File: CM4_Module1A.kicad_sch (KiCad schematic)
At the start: 1 part

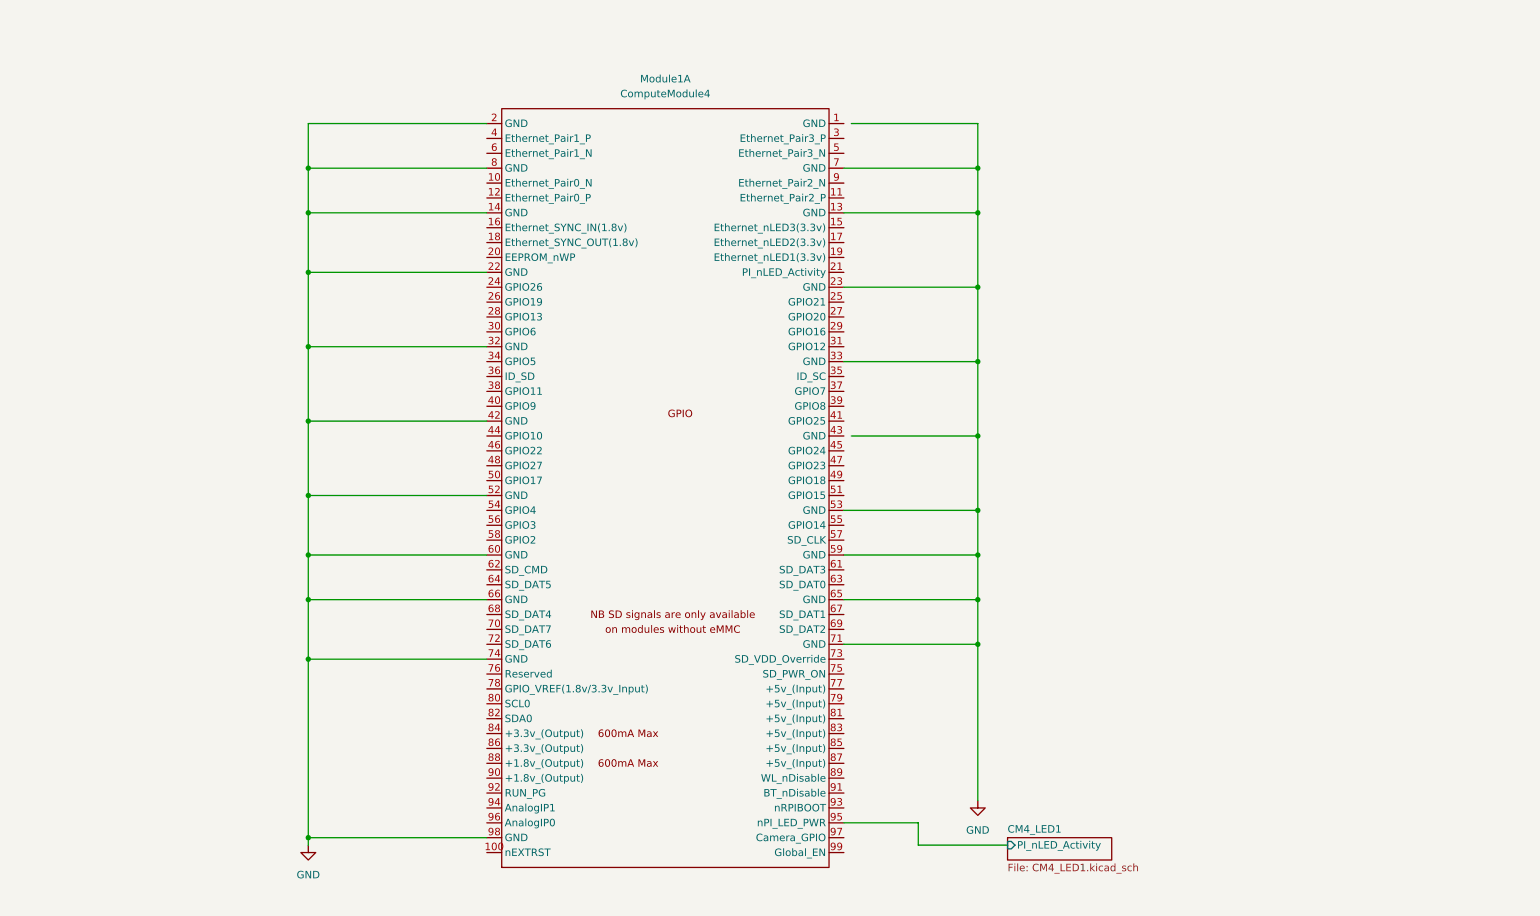
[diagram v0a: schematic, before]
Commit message: added gitignore, and did work on CM4
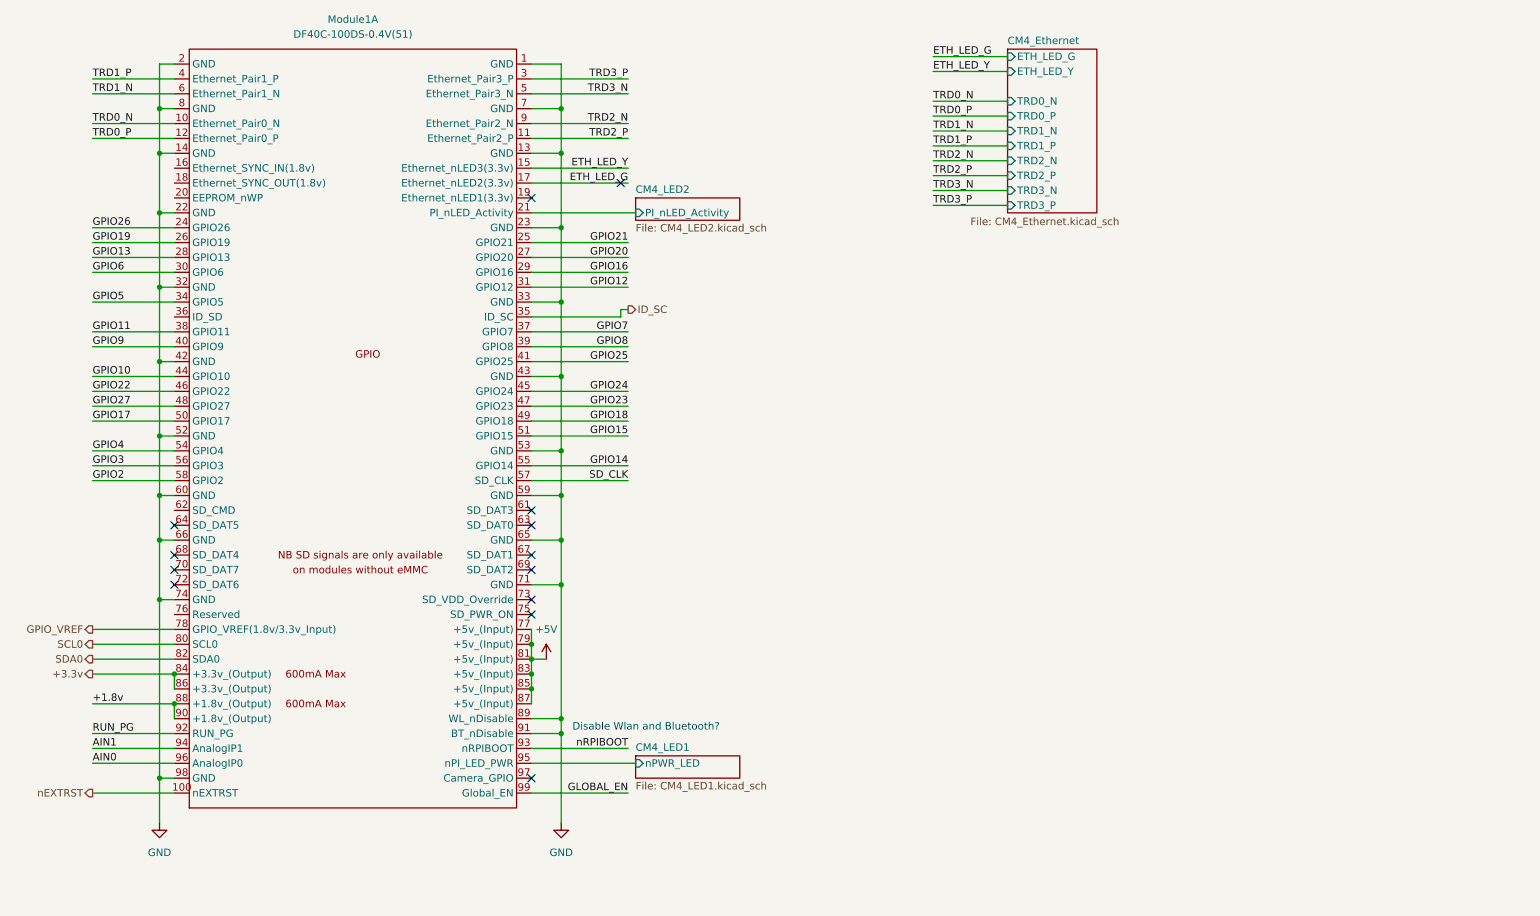
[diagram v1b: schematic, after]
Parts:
- removed Module1: ComputeModule4, CM4IO:Raspberry-Pi-4-Compute-Module, symbol dz_con:DF40C-100DS-0.4V_51_
- added Module1: DF40C-100DS-0.4V(51), dz_con:Con-Raspberry-Pi-4-Compute-Module, symbol #dzdb:s_con/CON-DF40C-100DS-0.4V51
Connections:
- net GND: now also Module1.1 (GND), Module1.13 (GND), Module1.14 (GND), Module1.2 (GND), Module1.22 (GND), Module1.23 (GND), Module1.32 (GND), Module1.33 (GND), Module1.42 (GND), Module1.43 (GND), Module1.52 (GND), Module1.53 (GND), Module1.59 (GND), Module1.60 (GND), Module1.65 (GND), Module1.66 (GND), Module1.7 (GND), Module1.71 (GND), Module1.74 (GND), Module1.8 (GND), Module1.89 (WL_nDisable), Module1.91 (BT_nDisable), Module1.98 (GND)
- new net +1.8v: Module1.88 (+1.8v_(Output)), Module1.90 (+1.8v_(Output))
- new net +3.3v: Module1.84 (+3.3v_(Output)), Module1.86 (+3.3v_(Output))
- new net +5V: Module1.77 (+5v_(Input)), Module1.79 (+5v_(Input)), Module1.81 (+5v_(Input)), Module1.83 (+5v_(Input)), Module1.85 (+5v_(Input)), Module1.87 (+5v_(Input))
- new net AIN0: Module1.96 (AnalogIP0)
- new net AIN1: Module1.94 (AnalogIP1)
- new net CM4_LED1/nPWR_LED: Module1.95 (nPI_LED_PWR)
- new net CM4_LED2/PI_nLED_Activity: Module1.21 (PI_nLED_Activity)
- new net ETH_LED_G: Module1.17 (Ethernet_nLED2(3.3v))
- new net ETH_LED_Y: Module1.15 (Ethernet_nLED3(3.3v))
- new net GLOBAL_EN: Module1.99 (Global_EN)
- new net GPIO10: Module1.44 (GPIO10)
- new net GPIO11: Module1.38 (GPIO11)
- new net GPIO12: Module1.31 (GPIO12)
- new net GPIO13: Module1.28 (GPIO13)
- new net GPIO14: Module1.55 (GPIO14)
- new net GPIO15: Module1.51 (GPIO15)
- new net GPIO16: Module1.29 (GPIO16)
- new net GPIO17: Module1.50 (GPIO17)
- new net GPIO18: Module1.49 (GPIO18)
- new net GPIO19: Module1.26 (GPIO19)
- new net GPIO2: Module1.58 (GPIO2)
- new net GPIO20: Module1.27 (GPIO20)
- new net GPIO21: Module1.25 (GPIO21)
- new net GPIO22: Module1.46 (GPIO22)
- new net GPIO23: Module1.47 (GPIO23)
- new net GPIO24: Module1.45 (GPIO24)
- new net GPIO25: Module1.41 (GPIO25)
- new net GPIO26: Module1.24 (GPIO26)
- new net GPIO27: Module1.48 (GPIO27)
- new net GPIO3: Module1.56 (GPIO3)
- new net GPIO4: Module1.54 (GPIO4)
- new net GPIO5: Module1.34 (GPIO5)
- new net GPIO6: Module1.30 (GPIO6)
- new net GPIO7: Module1.37 (GPIO7)
- new net GPIO8: Module1.39 (GPIO8)
- new net GPIO9: Module1.40 (GPIO9)
- new net GPIO_VREF: Module1.78 (GPIO_VREF(1.8v/3.3v_Input))
- new net ID_SC: Module1.35 (ID_SC)
- new net RUN_PG: Module1.92 (RUN_PG)
- new net SCL0: Module1.80 (SCL0)
- new net SDA0: Module1.82 (SDA0)
- new net SD_CLK: Module1.57 (SD_CLK)
- new net TRD0_N: Module1.10 (Ethernet_Pair0_N)
- new net TRD0_P: Module1.12 (Ethernet_Pair0_P)
- new net TRD1_N: Module1.6 (Ethernet_Pair1_N)
- new net TRD1_P: Module1.4 (Ethernet_Pair1_P)
- new net TRD2_N: Module1.9 (Ethernet_Pair2_N)
- new net TRD2_P: Module1.11 (Ethernet_Pair2_P)
- new net TRD3_N: Module1.5 (Ethernet_Pair3_N)
- new net TRD3_P: Module1.3 (Ethernet_Pair3_P)
- new net nEXTRST: Module1.100 (nEXTRST)
- new net nRPIBOOT: Module1.93 (nRPIBOOT)
- no-connect marks 0 -> 13
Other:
- added sheet CM4_Ethernet (CM4_Ethernet.kicad_sch)
- added sheet CM4_LED2 (CM4_LED2.kicad_sch)
- sheet CM4_LED1 ports: added nPWR_LED; removed PI_nLED_Activity
- note added: "Disable Wlan and Bluetooth?"

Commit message: minor changes/cleanup
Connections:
- net +1.8v renamed +1V8
- net +3.3v renamed +3.3V
- net TRD0_N renamed ET1
- net TRD0_P renamed ET2
- net TRD1_N renamed ET3
- net TRD1_P renamed ET4
- net TRD2_N renamed ET5
- net TRD2_P renamed ET6
- net TRD3_N renamed ET7
- net TRD3_P renamed ET8
- no-connect marks 13 -> 12

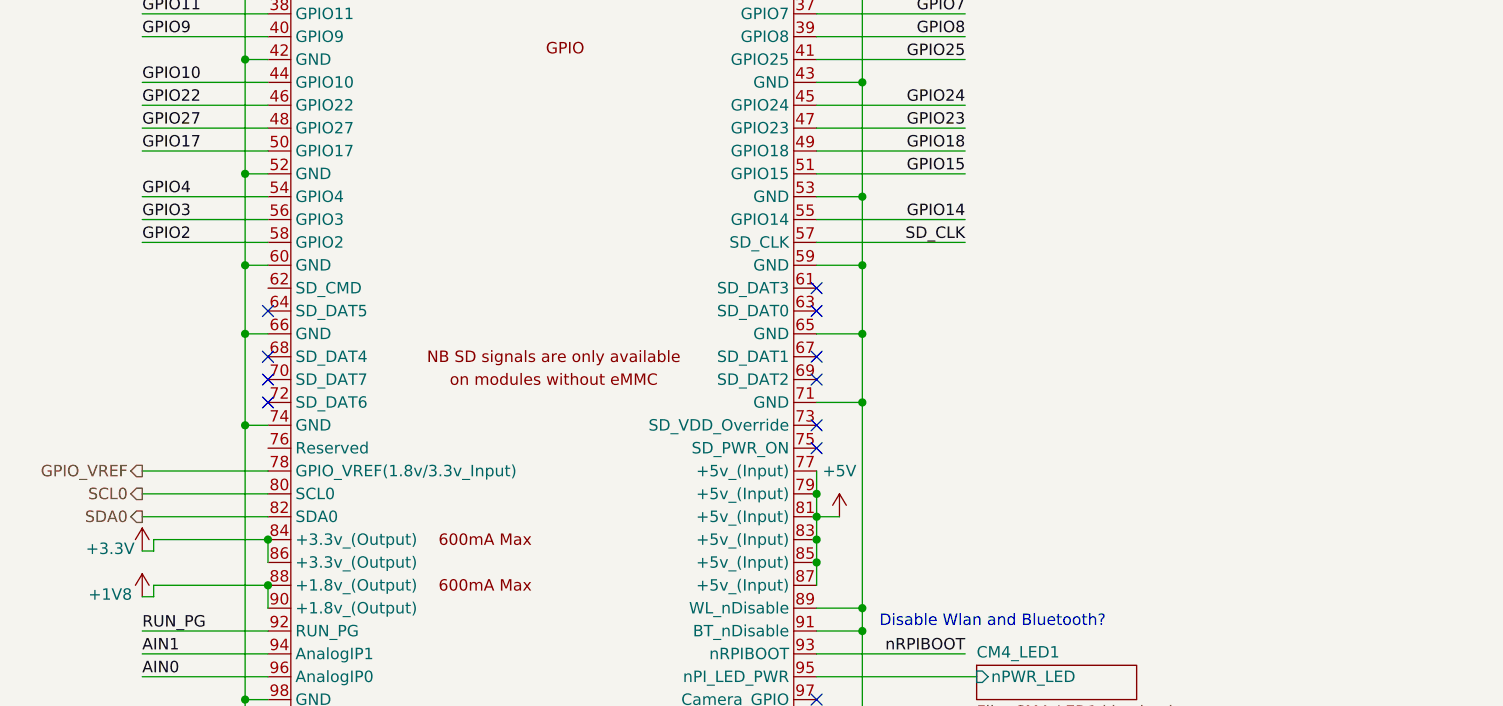
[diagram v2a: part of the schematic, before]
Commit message: readded RX and TX, Corrected DZ_PATHS to be relative instead of absolute.
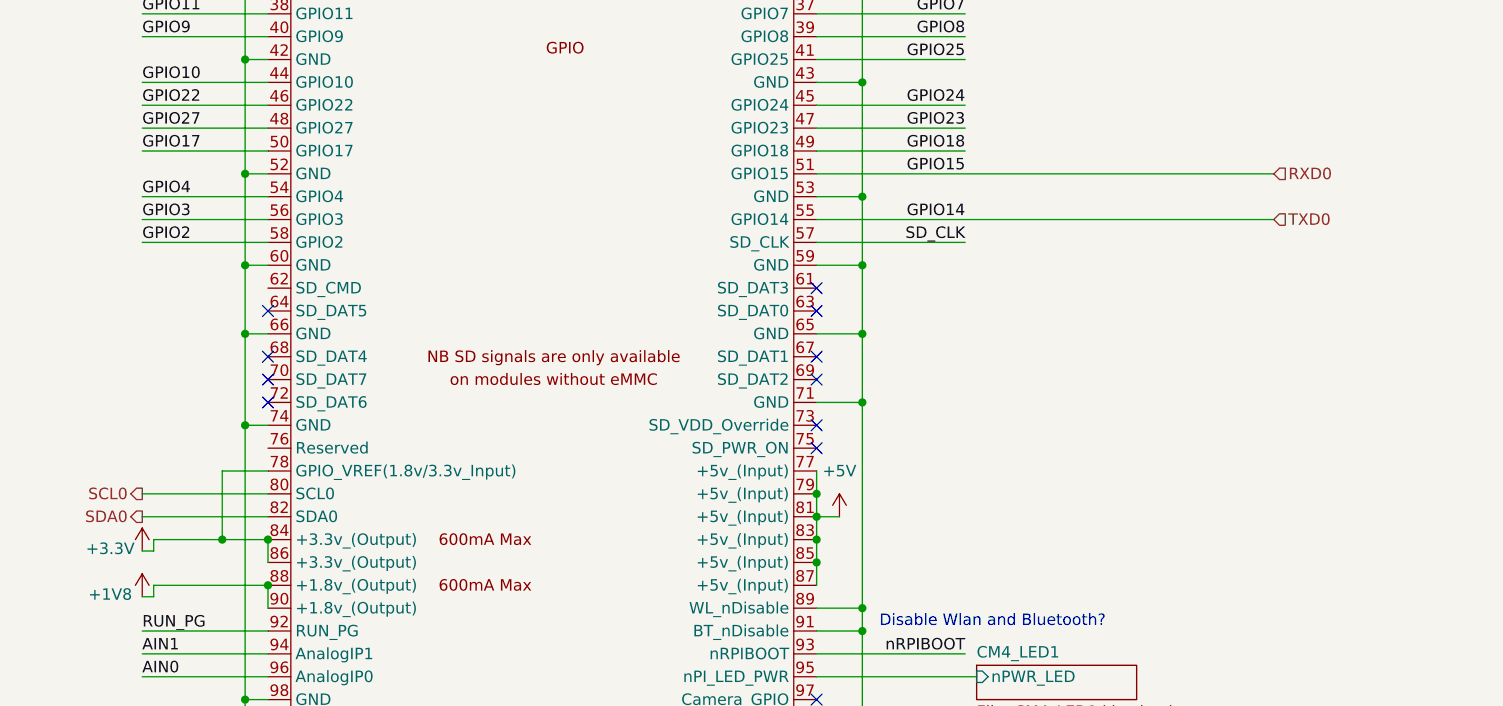
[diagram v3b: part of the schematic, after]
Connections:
- net GPIO_VREF is gone; now on net +3.3V: Module1.78 (GPIO_VREF(1.8v/3.3v_Input))
- net GPIO14 renamed TXD0
- net GPIO15 renamed RXD0
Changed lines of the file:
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@@
+	)
+	(junction
+		(at 35.56 128.27)
+		(diameter 0)
+		(color 0 0 0 0)
 	)
 	(junction
@@
 	(wire
 		(pts
-			(xy 101.6 92.71) (xy 118.11 92.71)
+			(xy 101.6 92.71) (xy 152.4 92.71)
 		)
 		(stroke
@@
 	(wire
 		(pts
+			(xy 35.56 128.27) (xy 40.64 128.27)
+		)
+		(stroke
+			(width 0)
+			(type default)
+		)
+	)
+	(wire
+		(pts
 			(xy 38.1 146.05) (xy 38.1 153.67)
 		)
@@
 	(wire
 		(pts
-			(xy 27.94 128.27) (xy 40.64 128.27)
+			(xy 27.94 128.27) (xy 35.56 128.27)
 		)
 		(stroke
@@
 	(wire
 		(pts
-			(xy 101.6 87.63) (xy 118.11 87.63)
+			(xy 101.6 87.63) (xy 152.4 87.63)
 		)
 		(stroke
@@
 	(wire
 		(pts
+			(xy 35.56 120.65) (xy 40.64 120.65)
+		)
+		(stroke
+			(width 0)
+			(type default)
+		)
+	)
+	(wire
+		(pts
 			(xy 185.42 38.1) (xy 201.93 38.1)
 		)
@@
 	(wire
 		(pts
+			(xy 35.56 128.27) (xy 35.56 120.65)
+		)
+		(stroke
+			(width 0)
+			(type default)
+		)
+	)
+	(wire
+		(pts
 			(xy 26.67 64.77) (xy 40.64 64.77)
 		)
@@
 		(pts
 			(xy 26.67 123.19) (xy 40.64 123.19)
-		)
-		(stroke
-			(width 0)
-			(type default)
-		)
-	)
-	(wire
-		(pts
-			(xy 26.67 120.65) (xy 40.64 120.65)
 		)
 		(stroke
@@
 		)
 	)
-	(hierarchical_label "GPIO_VREF"
-		(shape output)
-		(at 26.67 120.65 180)
-		(effects
-			(font
-				(size 1.27 1.27)
-			)
-			(justify right)
-		)
-	)
 	(hierarchical_label "ET4"
 		(shape input)
@@
 		)
 	)
+	(hierarchical_label "TXD0"
+		(shape input)
+		(at 152.4 92.71 0)
+		(effects
+			(font
+				(size 1.27 1.27)
+			)
+			(justify left)
+		)
+	)
 	(hierarchical_label "ET6"
 		(shape input)
@@
 		)
 	)
+	(hierarchical_label "RXD0"
+		(shape input)
+		(at 152.4 87.63 0)
+		(effects
+			(font
+				(size 1.27 1.27)
+			)
+			(justify left)
+		)
+	)

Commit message: Comments (+ new Connector?)
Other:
- note added: "Serial needs clock?"
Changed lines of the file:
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@@
 	(generator_version "9.0")
 	(paper "A4")
+	(text "Serial needs clock?\n"
+		(exclude_from_sim no)
+		(at 175.514 89.916 0)
+		(effects
+			(font
+				(size 1.27 1.27)
+			)
+		)
+	)
 	(text "Disable Wlan and Bluetooth?"
 		(exclude_from_sim no)

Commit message: Changed template of the sheet
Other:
- note added: "no."
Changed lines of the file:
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@@
 	(generator_version "9.0")
 	(paper "A4")
+	(text "no."
+		(exclude_from_sim no)
+		(at 173.228 92.202 0)
+		(effects
+			(font
+				(size 1.27 1.27)
+			)
+		)
+	)
 	(text "Serial needs clock?\n"
 		(exclude_from_sim no)

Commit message: WIFI connection changes PI
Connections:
- net GND: no longer Module1.89 (WL_nDisable)
- net +1V8: no longer names the net of Module1.88 (+1.8v_(Output)), Module1.90 (+1.8v_(Output))
- net +3.3V: no longer names the net of Module1.84 (+3.3v_(Output)), Module1.86 (+3.3v_(Output))
- net +3.3V: no longer Module1.78 (GPIO_VREF(1.8v/3.3v_Input))
- new net GPIO_VREF: Module1.78 (GPIO_VREF(1.8v/3.3v_Input))
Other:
- note added: "connect Wlan to gnd if off, and leave floating for on. Please use a 2 pin connector here with a jumper cap. (has to be done)"
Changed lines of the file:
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@@
+		)
+	)
+	(text "connect Wlan to gnd if off, and leave floating for on.\nPlease use a 2 pin connector here with a jumper cap. (has to be done)"
+		(exclude_from_sim no)
+		(at 148.844 121.158 0)
+		(effects
+			(font
+				(size 1.27 1.27)
+			)
 		)
 	)
@@
 	)
 	(junction
-		(at 40.64 133.35)
-		(diameter 0)
-		(color 0 0 0 0)
-	)
-	(junction
 		(at 106.68 64.77)
 		(diameter 0)
@@
 	)
 	(junction
-		(at 106.68 135.89)
-		(diameter 0)
-		(color 0 0 0 0)
-	)
-	(junction
 		(at 38.1 115.57)
 		(diameter 0)
@@
 	)
 	(junction
-		(at 35.56 128.27)
-		(diameter 0)
-		(color 0 0 0 0)
-	)
-	(junction
 		(at 101.6 125.73)
 		(diameter 0)
@@
 	)
 	(junction
+		(at 106.68 129.54)
+		(diameter 0)
+		(color 0 0 0 0)
+	)
+	(junction
 		(at 101.6 130.81)
 		(diameter 0)
@@
 	)
 	(junction
-		(at 40.64 128.27)
-		(diameter 0)
-		(color 0 0 0 0)
-	)
-	(junction
 		(at 38.1 105.41)
 		(diameter 0)
@@
 	(wire
 		(pts
+			(xy 106.68 129.54) (xy 106.68 138.43)
+		)
+		(stroke
+			(width 0)
+			(type default)
+		)
+	)
+	(wire
+		(pts
 			(xy 101.6 130.81) (xy 101.6 133.35)
 		)
@@
 	(wire
 		(pts
+			(xy 101.6 135.89) (xy 123.19 124.46)
+		)
+		(stroke
+			(width 0)
+			(type default)
+		)
+	)
+	(wire
+		(pts
 			(xy 101.6 92.71) (xy 152.4 92.71)
 		)
@@
 	(wire
 		(pts
-			(xy 35.56 128.27) (xy 40.64 128.27)
+			(xy 106.68 129.54) (xy 120.65 124.46)
 		)
 		(stroke
@@
 	(wire
 		(pts
-			(xy 27.94 133.35) (xy 40.64 133.35)
-		)
-		(stroke
-			(width 0)
-			(type default)
-		)
-	)
-	(wire
-		(pts
 			(xy 101.6 44.45) (xy 118.11 44.45)
 		)
@@
 	(wire
 		(pts
-			(xy 101.6 135.89) (xy 106.68 135.89)
-		)
-		(stroke
-			(width 0)
-			(type default)
-		)
-	)
-	(wire
-		(pts
 			(xy 26.67 59.69) (xy 40.64 59.69)
 		)
@@
 	(wire
 		(pts
-			(xy 27.94 128.27) (xy 35.56 128.27)
-		)
-		(stroke
-			(width 0)
-			(type default)
-		)
-	)
-	(wire
-		(pts
 			(xy 38.1 74.93) (xy 38.1 87.63)
 		)
@@
 	(wire
 		(pts
-			(xy 35.56 120.65) (xy 40.64 120.65)
+			(xy 26.67 120.65) (xy 40.64 120.65)
 		)
 		(stroke
@@
 	(wire
 		(pts
-			(xy 27.94 129.54) (xy 27.94 128.27)
-		)
-		(stroke
-			(width 0)
-			(type default)
-		)
-	)
-	(wire
-		(pts
 			(xy 116.84 67.31) (xy 101.6 67.31)
 		)
@@
 	(wire
 		(pts
-			(xy 35.56 128.27) (xy 35.56 120.65)
-		)
-		(stroke
-			(width 0)
-			(type default)
-		)
-	)
-	(wire
-		(pts
 			(xy 26.67 64.77) (xy 40.64 64.77)
 		)
@@
 	(wire
 		(pts
-			(xy 106.68 135.89) (xy 106.68 138.43)
+			(xy 106.68 113.03) (xy 106.68 129.54)
 		)
 		(stroke
@@
 	(wire
 		(pts
-			(xy 27.94 134.62) (xy 27.94 133.35)
-		)
-		(stroke
-			(width 0)
-			(type default)
-		)
-	)
-	(wire
-		(pts
 			(xy 40.64 39.37) (xy 38.1 39.37)
 		)
@@
 	(wire
 		(pts
-			(xy 26.67 129.54) (xy 27.94 129.54)
-		)
-		(stroke
-			(width 0)
-			(type default)
-		)
-	)
-	(wire
-		(pts
 			(xy 38.1 24.13) (xy 38.1 31.75)
 		)
@@
 	(wire
 		(pts
-			(xy 106.68 113.03) (xy 106.68 135.89)
-		)
-		(stroke
-			(width 0)
-			(type default)
-		)
-	)
-	(wire
-		(pts
 			(xy 26.67 26.67) (xy 40.64 26.67)
 		)
@@
 		(pts
 			(xy 101.6 128.27) (xy 101.6 130.81)
-		)
-		(stroke
-			(width 0)
-			(type default)
-		)
-	)
-	(wire
-		(pts
-			(xy 26.67 134.62) (xy 27.94 134.62)
 		)
 		(stroke
@@
 		(shape input)
 		(at 185.42 33.02 180)
+		(effects
+			(font
+				(size 1.27 1.27)
+			)
+			(justify right)
+		)
+	)
+	(hierarchical_label "GPIO_VREF"
+		(shape input)
+		(at 26.67 120.65 180)
 		(effects
 			(font
@@
 					(unit 1)
 				)
-			)
-		)
-	)
-	(symbol
-		(lib_id "power:+1V8")
-		(at 26.67 134.62 0)
-		(unit 1)
-		(exclude_from_sim no)
-		(in_bom yes)
-		(on_board yes)
-		(dnp no)
-		(property "Reference" "#PWR03"
-			(at 26.67 138.43 0)
-			(effects
-				(font
-					(size 1.27 1.27)
-				)
-				(hide yes)
-			)
-		)
-		(property "Value" "+1V8"
-			(at 23.114 134.366 0)
-			(effects
-				(font
-					(size 1.27 1.27)
-				)
-			)
-		)
-		(property "Footprint" ""
-			(at 26.67 134.62 0)
-			(effects
-				(font
-					(size 1.27 1.27)
-				)
-				(hide yes)
-			)
-		)
-		(property "Datasheet" ""
-			(at 26.67 134.62 0)
-			(effects
-				(font
-					(size 1.27 1.27)
-				)
-				(hide yes)
-			)
-		)
-		(property "Description" "Power symbol creates a global label with name \"+1V8\""
-			(at 26.67 134.62 0)
-			(effects
-				(font
-					(size 1.27 1.27)
-				)
-				(hide yes)
-			)
-		)
-		(pin "1"
-		)
-		(instances
-			(project "nautilus_mainboard"
-				(path "/ce1819b2-f280-40ed-834f-6fe4d12f809d/c2b6dac3-d6fd-4d5d-bd17-0cff91db88eb/0837dad1-ec16-488a-a684-981e55247089"
-					(reference "#PWR03")
-					(unit 1)
-				)
-			)
-		)
-	)
-	(symbol
-		(lib_id "power:+3.3V")
-		(at 26.67 129.54 0)
-		(unit 1)
-		(exclude_from_sim no)
-		(in_bom yes)
-		(on_board yes)
-		(dnp no)
-		(property "Reference" "#PWR02"
-			(at 26.67 133.35 0)
-			(effects
-				(font
-					(size 1.27 1.27)
-				)
-				(hide yes)
-			)
-		)
-		(property "Value" "+3.3V"
-			(at 23.114 129.286 0)
-			(effects
-				(font
-					(size 1.27 1.27)
-				)
-			)
-		)
-		(property "Footprint" ""
-			(at 26.67 129.54 0)
-			(effects
-				(font
-					(size 1.27 1.27)
-				)
-				(hide yes)
-			)
-		)
-		(property "Datasheet" ""
-			(at 26.67 129.54 0)
-			(effects
-				(font
-					(size 1.27 1.27)
-				)
-				(hide yes)
-			)
-		)
-		(property "Description" "Power symbol creates a global label with name \"+3.3V\""
-			(at 26.67 129.54 0)
-			(effects
-				(font
-					(size 1.27 1.27)
-				)
-				(hide yes)
-			)
-		)
-		(pin "1"
-		)
-		(instances
-			(project "nautilus_mainboard"
-				(path "/ce1819b2-f280-40ed-834f-6fe4d12f809d/c2b6dac3-d6fd-4d5d-bd17-0cff91db88eb/0837dad1-ec16-488a-a684-981e55247089"
-					(reference "#PWR02")
-					(unit 1)
-				)
